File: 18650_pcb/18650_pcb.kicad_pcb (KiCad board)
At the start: 2 copper layers, 40 x 88 mm, 5 parts, among them P1 CONN_01X02

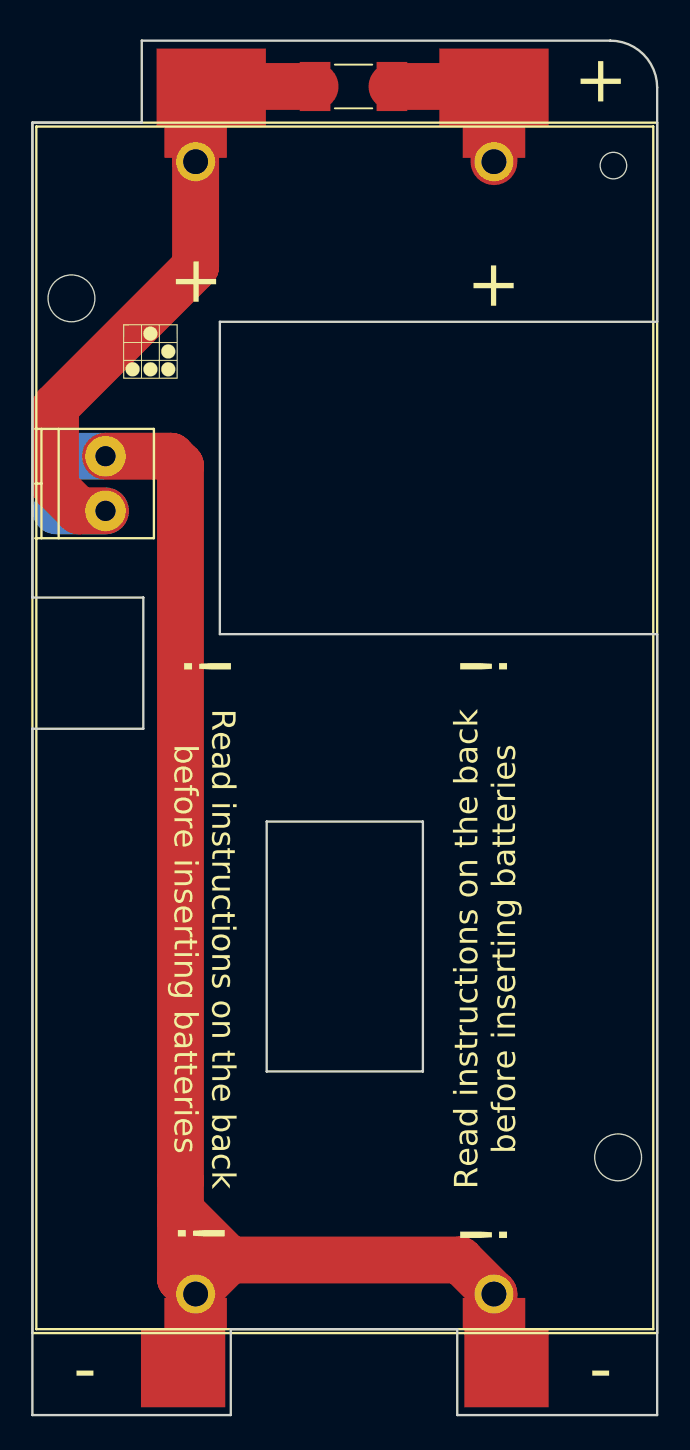
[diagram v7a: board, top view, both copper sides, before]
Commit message: Adjusted 18650 board outline, routing and silk to match the back board
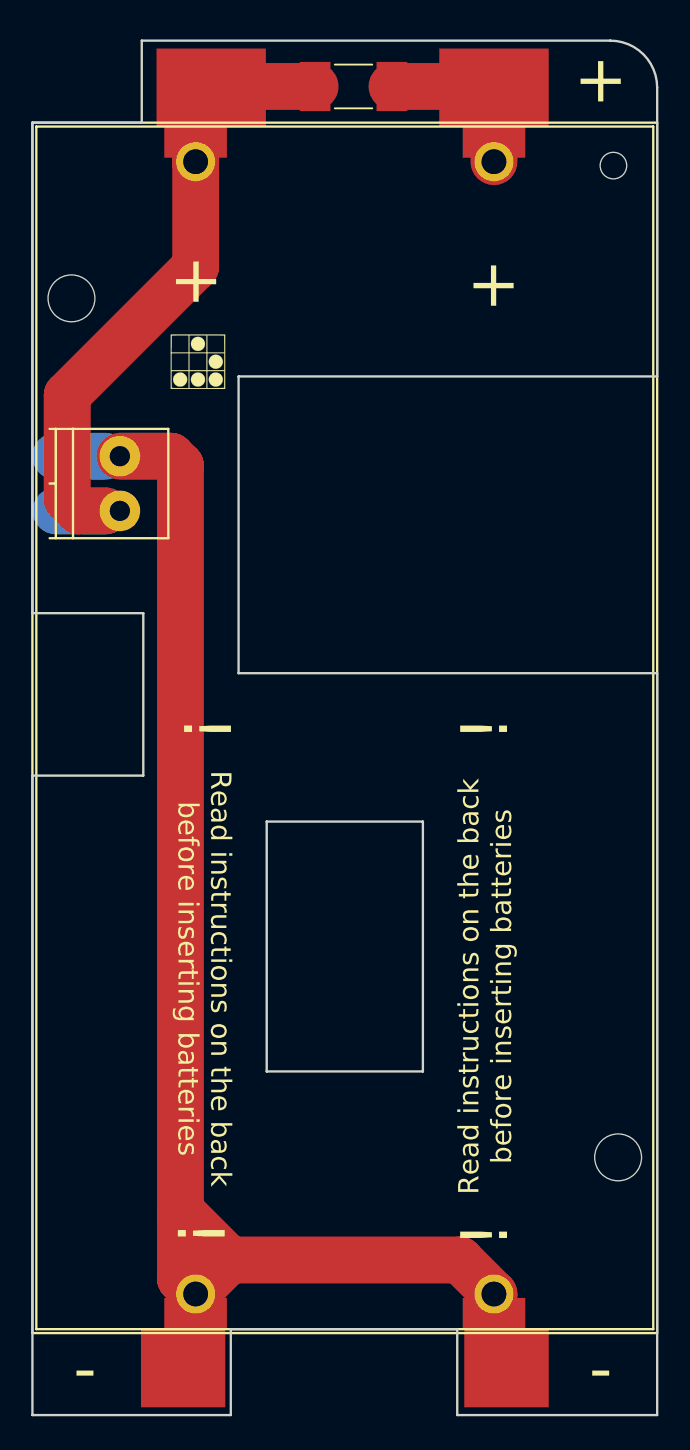
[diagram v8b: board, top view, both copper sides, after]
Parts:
- moved G*** 3.11 mm to (30.4, 37.8)
- moved P1 0.92 mm to (25.4, 43.8)
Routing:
- net Net-(BT1-Pad3): track 100.8 -> 99.8 mm
- net Net-(BT1-Pad1): track 43.0 -> 42.4 mm
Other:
- outline, holes or cut-outs redrawn
- board text added: "1. Remove microSD&nanoSIM cards 2. Insert first battery, charge it fully through microUSB (blue light = full) 3. Remove first battery 4. Charge second battery 5. Insert first battery"
- board text removed: "1. Remove microSD&nanoSIM cards 2. Insert first battery, charge it fully through microUSB (blue light = full) 3. Remove first battery 4. Insert second battery, charge fully 5. Insert first battery"
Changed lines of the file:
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@@
     (area 19.724019 17.124999 59.875001 105.275001)
     (thickness 1.6)
-    (drawings 55)
-    (tracks 27)
+    (drawings 54)
+    (tracks 26)
     (zones 0)
     (modules 5)
@@
   )
   (module Terminal_Blocks:TerminalBlock_Pheonix_PT-3.5mm_2pol (layer F.Cu)
-    (at 24.47862 43.80804 270)
+    (at 25.39902 43.80804 270)
     (descr "2-way 3.5mm pitch terminal block, Phoenix PT series")
     (fp_text reference P1 (at 1.75 -4.3 270) (layer F.SilkS) hide
@@
   )
   (module art:glider (layer F.Cu)
-    (at 27.35502 37.10124)
+    (at 30.39902 37.75724)
     (fp_text reference G*** (at 0 0) (layer F.SilkS) hide
       (effects (font (thickness 0.3)))
@@
   )
   (gr_line (start 26.8 22.45) (end 26.8 17.2) (layer Edge.Cuts) (width 0.15))
-  (gr_text ! (at 48.79902 57.25724 90) (layer F.SilkS)
+  (gr_text ! (at 48.79902 61.25724 90) (layer F.SilkS)
     (effects (font (size 3 3) (thickness 0.75)))
   )
@@
     (effects (font (size 3 3) (thickness 0.75)))
   )
-  (gr_text ! (at 30.89902 57.25724 270) (layer F.SilkS)
+  (gr_text ! (at 30.89902 61.25724 270) (layer F.SilkS)
     (effects (font (size 3 3) (thickness 0.75)))
   )
-  (gr_text "Read instructions on the back\nbefore inserting batteries" (at 30.79902 75.35724 270) (layer F.SilkS)
-    (effects (font (size 1.5 1.5) (thickness 0.3)))
-  )
-  (gr_text "Read instructions on the back\nbefore inserting batteries" (at 48.79902 75.35724 90) (layer F.SilkS)
-    (effects (font (size 1.5 1.5) (thickness 0.3)))
-  )
-  (gr_line (start 19.79902 61.25724) (end 19.79902 105.2) (layer Edge.Cuts) (width 0.15))
-  (gr_line (start 19.79902 22.45) (end 19.79902 52.85724) (layer Edge.Cuts) (width 0.15))
-  (gr_line (start 26.89902 61.25724) (end 19.79902 61.25724) (layer Edge.Cuts) (width 0.15))
-  (gr_line (start 26.89902 52.85724) (end 26.89902 61.25724) (layer Edge.Cuts) (width 0.15))
-  (gr_line (start 19.79902 52.85724) (end 26.89902 52.85724) (layer Edge.Cuts) (width 0.15))
+  (gr_text "Read instructions on the back\nbefore inserting batteries" (at 30.79902 77.25724 270) (layer F.SilkS)
+    (effects (font (size 1.3 1.3) (thickness 0.3)))
+  )
+  (gr_text "Read instructions on the back\nbefore inserting batteries" (at 48.79902 77.75724 90) (layer F.SilkS)
+    (effects (font (size 1.3 1.3) (thickness 0.3)))
+  )
+  (gr_line (start 19.79902 64.25724) (end 19.79902 105.2) (layer Edge.Cuts) (width 0.15))
+  (gr_line (start 19.79902 22.45) (end 19.79902 53.85724) (layer Edge.Cuts) (width 0.15))
+  (gr_line (start 26.89902 64.25724) (end 19.79902 64.25724) (layer Edge.Cuts) (width 0.15))
+  (gr_line (start 26.89902 53.85724) (end 26.89902 64.25724) (layer Edge.Cuts) (width 0.15))
+  (gr_line (start 19.79902 53.85724) (end 26.89902 53.85724) (layer Edge.Cuts) (width 0.15))
   (gr_text ---> (at 29.38702 80.02724 110) (layer B.SilkS)
     (effects (font (size 1.5 1.5) (thickness 0.3)) (justify mirror))
@@
     (effects (font (size 0.8 0.8) (thickness 0.15)) (justify mirror))
   )
-  (gr_text BAT+ (at 28.87902 47.51524) (layer B.SilkS)
+  (gr_text BAT+ (at 29.89902 47.25724) (layer B.SilkS)
     (effects (font (size 1.5 1.5) (thickness 0.3)) (justify mirror))
   )
@@
     (effects (font (size 0.9 0.9) (thickness 0.2)) (justify mirror))
   )
-  (gr_text BAT- (at 28.87902 44.21324) (layer B.SilkS)
+  (gr_text BAT- (at 29.89902 44.21324) (layer B.SilkS)
     (effects (font (size 1.5 1.5) (thickness 0.3)) (justify mirror))
   )
@@
     (effects (font (size 1 1) (thickness 0.2)) (justify mirror))
   )
-  (gr_text "1. Remove microSD&nanoSIM cards\n2. Insert first battery, charge it fully\nthrough microUSB (blue light = full)\n3. Remove first battery\n4. Insert second battery, charge fully\n5. Insert first battery" (at 41.89902 61.45724) (layer B.SilkS)
-    (effects (font (size 1 1) (thickness 0.2)) (justify mirror))
+  (gr_text "1. Remove microSD&nanoSIM cards\n2. Insert first battery, charge it fully\nthrough microUSB (blue light = full)\n3. Remove first battery\n4. Charge second battery\n5. Insert first battery" (at 40.14902 62.50724) (layer B.SilkS)
+    (effects (font (size 0.8 0.8) (thickness 0.15)) (justify mirror))
   )
   (gr_text - (at 56.18402 102.25224) (layer F.SilkS)
@@
     (effects (font (size 2 2) (thickness 0.4)) (justify mirror))
   )
-  (target plus (at 61.89902 15.25724) (size 5) (width 0.15) (layer Edge.Cuts))
   (gr_line (start 26.8 22.45) (end 19.8 22.45) (layer Edge.Cuts) (width 0.15))
   (gr_line (start 34.8 67.2) (end 34.8 83.2) (layer Edge.Cuts) (width 0.15))
@@
   (gr_line (start 44.8 67.2) (end 44.8 83.2) (layer Edge.Cuts) (width 0.15))
   (gr_line (start 34.8 67.2) (end 44.8 67.2) (layer Edge.Cuts) (width 0.15))
-  (gr_line (start 59.8 105.2) (end 59.8 55.2) (layer Edge.Cuts) (width 0.15))
-  (gr_line (start 31.8 55.2) (end 59.8 55.2) (layer Edge.Cuts) (width 0.15))
-  (gr_line (start 31.8 35.2) (end 31.8 55.2) (layer Edge.Cuts) (width 0.15))
-  (gr_line (start 31.8 35.2) (end 59.8 35.2) (layer Edge.Cuts) (width 0.15))
+  (gr_line (start 59.8 105.2) (end 59.8 57.7) (layer Edge.Cuts) (width 0.15))
+  (gr_line (start 33 57.7) (end 59.8 57.7) (layer Edge.Cuts) (width 0.15))
+  (gr_line (start 33 38.7) (end 33 57.7) (layer Edge.Cuts) (width 0.15))
+  (gr_line (start 33 38.7) (end 59.8 38.7) (layer Edge.Cuts) (width 0.15))
   (gr_arc (start 56.8 20.2) (end 56.8 17.2) (angle 90) (layer Edge.Cuts) (width 0.15))
   (gr_line (start 32.5 105.2) (end 19.8 105.2) (layer Edge.Cuts) (width 0.15))
@@
   (gr_line (start 47 99.7) (end 47 105.2) (layer Edge.Cuts) (width 0.15))
   (gr_line (start 59.8 105.2) (end 47 105.2) (layer Edge.Cuts) (width 0.15))
-  (gr_line (start 59.8 35.2) (end 59.8 20.2) (layer Edge.Cuts) (width 0.15))
+  (gr_line (start 59.8 38.7) (end 59.8 20.2) (layer Edge.Cuts) (width 0.15))
   (gr_line (start 26.8 17.2) (end 56.8 17.2) (layer Edge.Cuts) (width 0.15))
+  (segment (start 24.47862 47.30804) (end 22.781564 47.30804) (width 3) (layer F.Cu) (net 1))
+  (segment (start 22.781564 47.30804) (end 22.028182 46.554658) (width 3) (layer F.Cu) (net 1))
+  (segment (start 22.028182 46.554658) (end 22.028182 39.888078) (width 3) (layer F.Cu) (net 1))
+  (segment (start 22.028182 39.888078) (end 30.25 31.66626) (width 3) (layer F.Cu) (net 1))
+  (segment (start 30.25 31.66626) (end 30.25 24.95) (width 3) (layer F.Cu) (net 1))
   (segment (start 24.47862 47.30804) (end 21.30582 47.30804) (width 3) (layer B.Cu) (net 1))
   (segment (start 37.89982 20.13404) (end 31.31596 20.13404) (width 3) (layer F.Cu) (net 1))
   (segment (start 31.31596 20.13404) (end 31.25 20.2) (width 3) (layer F.Cu) (net 1))
-  (segment (start 21.27861 40.63765) (end 30.25 31.66626) (width 3) (layer F.Cu) (net 1))
-  (segment (start 30.25 31.66626) (end 30.25 24.95) (width 3) (layer F.Cu) (net 1))
-  (segment (start 24.47862 47.30804) (end 22.781564 47.30804) (width 3) (layer F.Cu) (net 1))
-  (segment (start 21.27861 45.805086) (end 21.27861 40.63765) (width 3) (layer F.Cu) (net 1))
-  (segment (start 22.781564 47.30804) (end 21.27861 45.805086) (width 3) (layer F.Cu) (net 1))
   (segment (start 30.25 20.2) (end 30.25 24.95) (width 3) (layer F.Cu) (net 1))
+  (segment (start 29.27862 92.72724) (end 29.27862 44.40804) (width 3) (layer F.Cu) (net 2))
+  (segment (start 29.27862 44.40804) (end 28.67862 43.80804) (width 3) (layer F.Cu) (net 2))
+  (segment (start 28.67862 43.80804) (end 25.39902 43.80804) (width 3) (layer F.Cu) (net 2))
   (segment (start 24.47862 43.80804) (end 21.28322 43.80804) (width 3) (layer B.Cu) (net 2))
-  (segment (start 29.27862 90.18724) (end 29.27862 92.72724) (width 3) (layer F.Cu) (net 2))
-  (segment (start 29.27862 44.40804) (end 29.27862 90.18724) (width 3) (layer F.Cu) (net 2))
   (segment (start 29.27862 92.1131) (end 32.43276 95.26724) (width 3) (layer F.Cu) (net 2))
   (segment (start 29.27862 92.72724) (end 29.27862 96.47862) (width 3) (layer F.Cu) (net 2))
@@
   (segment (start 32.43276 95.26724) (end 47.16724 95.26724) (width 3) (layer F.Cu) (net 2))
   (segment (start 30.25 97.45) (end 32.43276 95.26724) (width 3) (layer F.Cu) (net 2))
-  (segment (start 24.47862 43.80804) (end 28.67862 43.80804) (width 3) (layer F.Cu) (net 2))
-  (segment (start 28.67862 43.80804) (end 29.27862 44.40804) (width 3) (layer F.Cu) (net 2))
   (segment (start 29.27862 96.47862) (end 30.25 97.45) (width 3) (layer F.Cu) (net 2))
   (segment (start 49.35 97.45) (end 49.35 102.2) (width 3) (layer F.Cu) (net 2))
